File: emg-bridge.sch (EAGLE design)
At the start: 23 parts

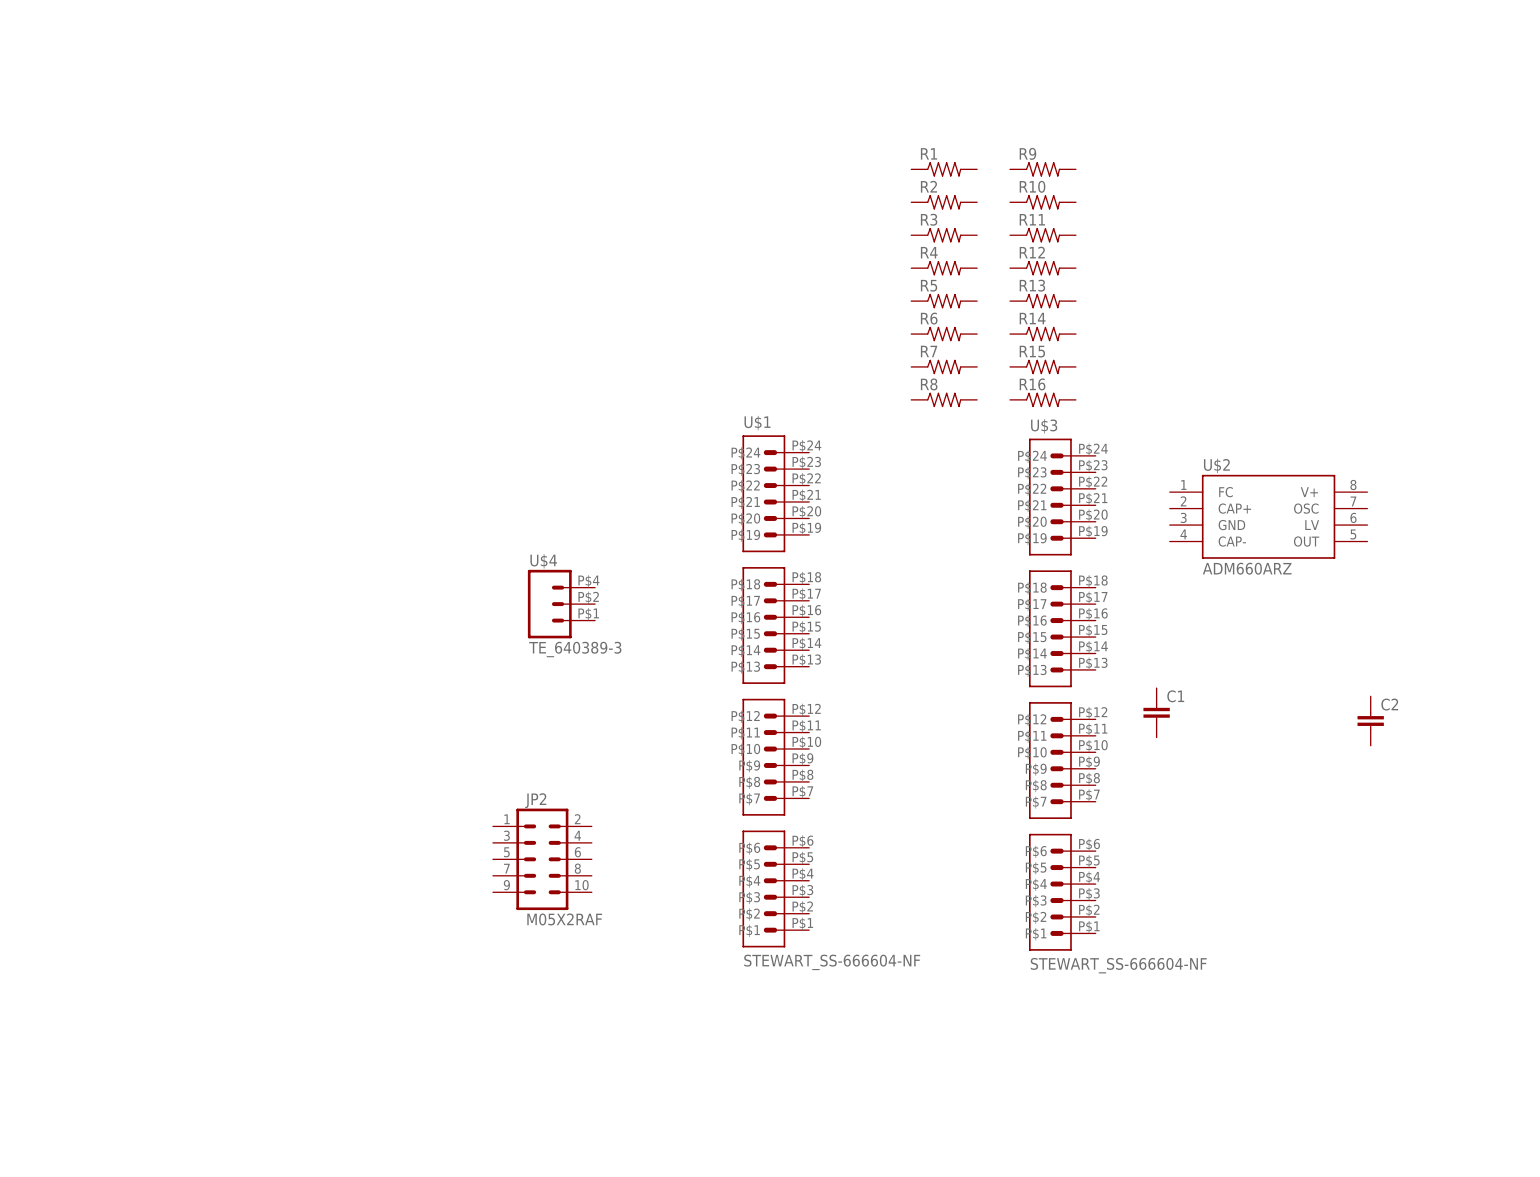
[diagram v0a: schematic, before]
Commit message: Updated parts from eagle-lib. Worked out pinouts for all connectors.
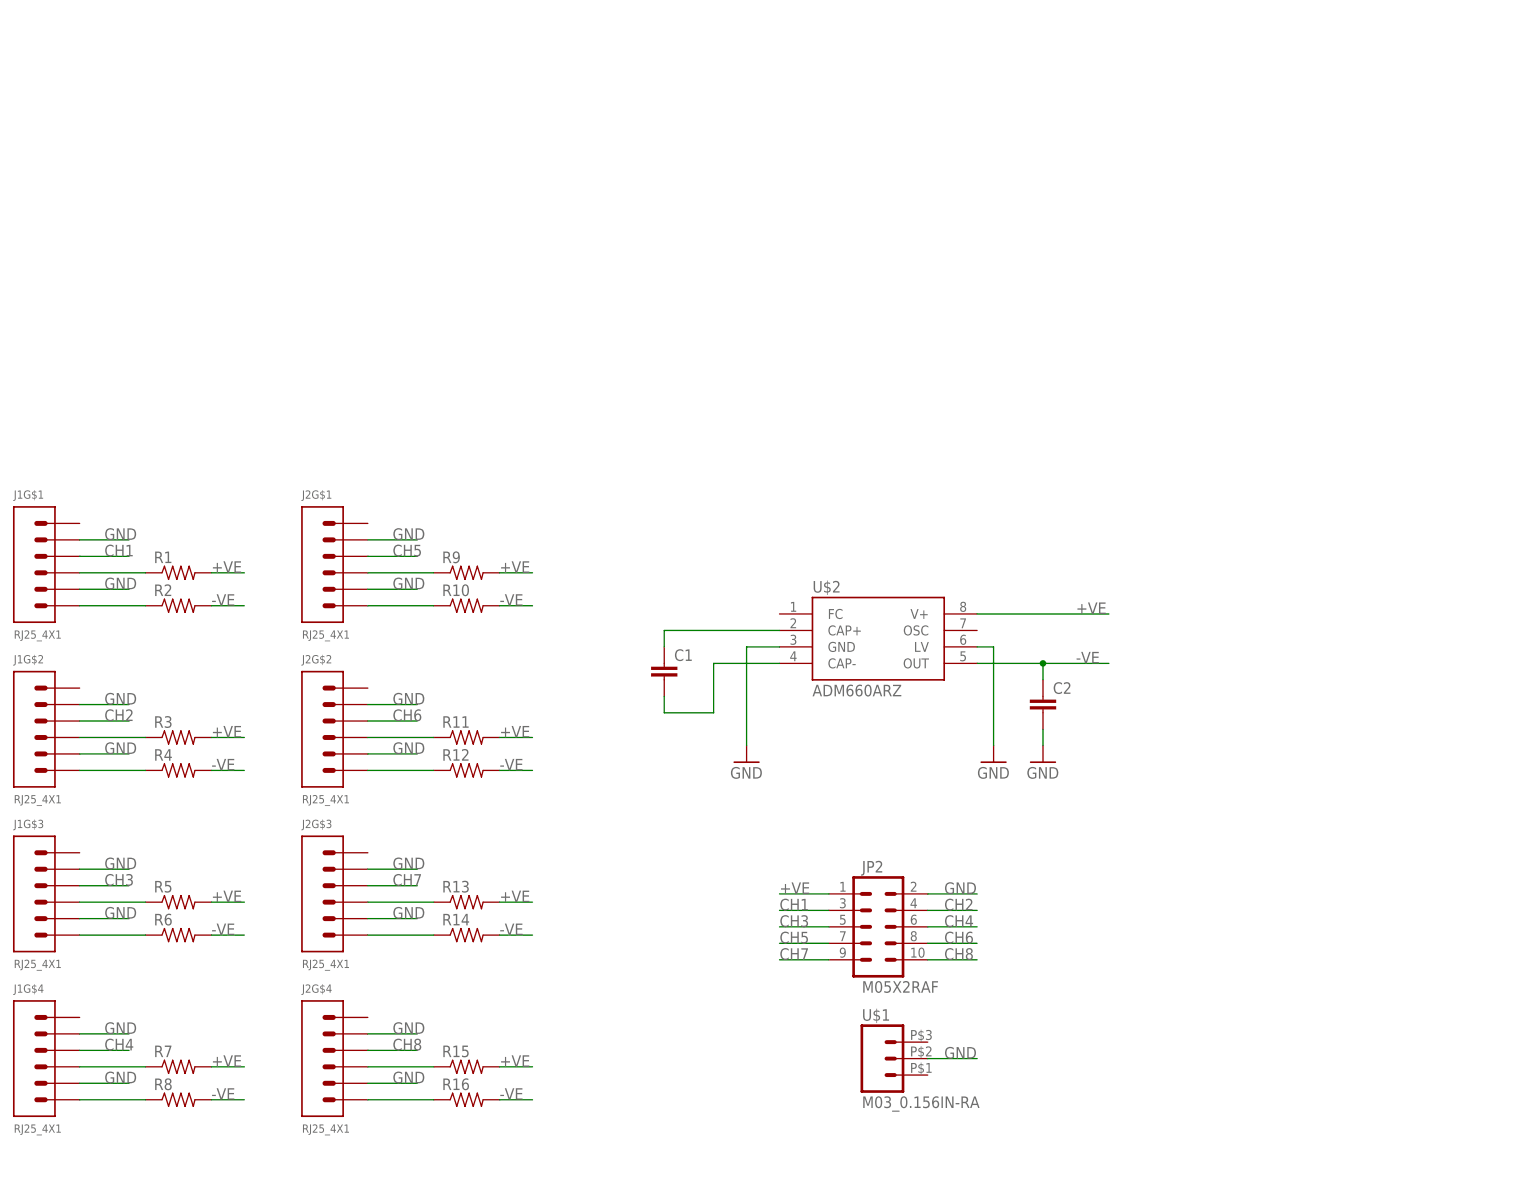
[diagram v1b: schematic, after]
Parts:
- removed U$3: STEWART_SS-666604-NF, eagle-lib:STEWART_SS-666604-NF
- removed U$4: TE_640389-3, eagle-lib:TE_640389-3
- added J1, J2: RJ25_4X1, eagle-lib:RJ25_4X1
- U$1: value STEWART_SS-666604-NF -> M03_0.156IN-RA; device eagle-lib:STEWART_SS-666604-NF -> eagle-lib:M03_0.156IN-RA
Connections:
- new net +VE: JP2.1, R1.2, R11.2, R13.2, R15.2, R3.2, R5.2, R7.2, R9.2, U$2.V+
- new net -VE: C2.1, R10.2, R12.2, R14.2, R16.2, R2.2, R4.2, R6.2, R8.2, U$2.OUT
- new net CH1: J1G$1.P$4, JP2.3
- new net CH2: J1G$2.P$4, JP2.4
- new net CH3: J1G$3.P$4, JP2.5
- new net CH4: J1G$4.P$4, JP2.6
- new net CH5: J2G$1.P$4, JP2.7
- new net CH6: J2G$2.P$4, JP2.8
- new net CH7: J2G$3.P$4, JP2.9
- new net CH8: J2G$4.P$4, JP2.10
- new net GND: C2.2, J1G$1.P$2, J1G$1.P$5, J1G$2.P$2, J1G$2.P$5, J1G$3.P$2, J1G$3.P$5, J1G$4.P$2, J1G$4.P$5, J2G$1.P$2, J2G$1.P$5, J2G$2.P$2, J2G$2.P$5, J2G$3.P$2, J2G$3.P$5, J2G$4.P$2, J2G$4.P$5, JP2.2, U$1.2, U$2.GND, U$2.LV
- new net N$1: J1G$1.P$1, R2.1
- new net N$11: J1G$3.P$1, R6.1
- new net N$13: J1G$3.P$3, R5.1
- new net N$16: J1G$4.P$1, R8.1
- new net N$18: J1G$4.P$3, R7.1
- new net N$2: C1.2, U$2.CAP-
- new net N$21: J2G$1.P$1, R10.1
- new net N$23: J2G$1.P$3, R9.1
- new net N$26: J2G$2.P$1, R12.1
- new net N$28: J2G$2.P$3, R11.1
- new net N$3: J1G$1.P$3, R1.1
- new net N$31: J2G$3.P$1, R14.1
- new net N$33: J2G$3.P$3, R13.1
- new net N$36: J2G$4.P$1, R16.1
- new net N$38: J2G$4.P$3, R15.1
- new net N$4: C1.1, U$2.CAP+
- new net N$6: J1G$2.P$1, R4.1
- new net N$8: J1G$2.P$3, R3.1
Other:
- moved on the sheet: C1, C2, JP2, R1, R10, R11, R12, R13, R14, R15, R16, R2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

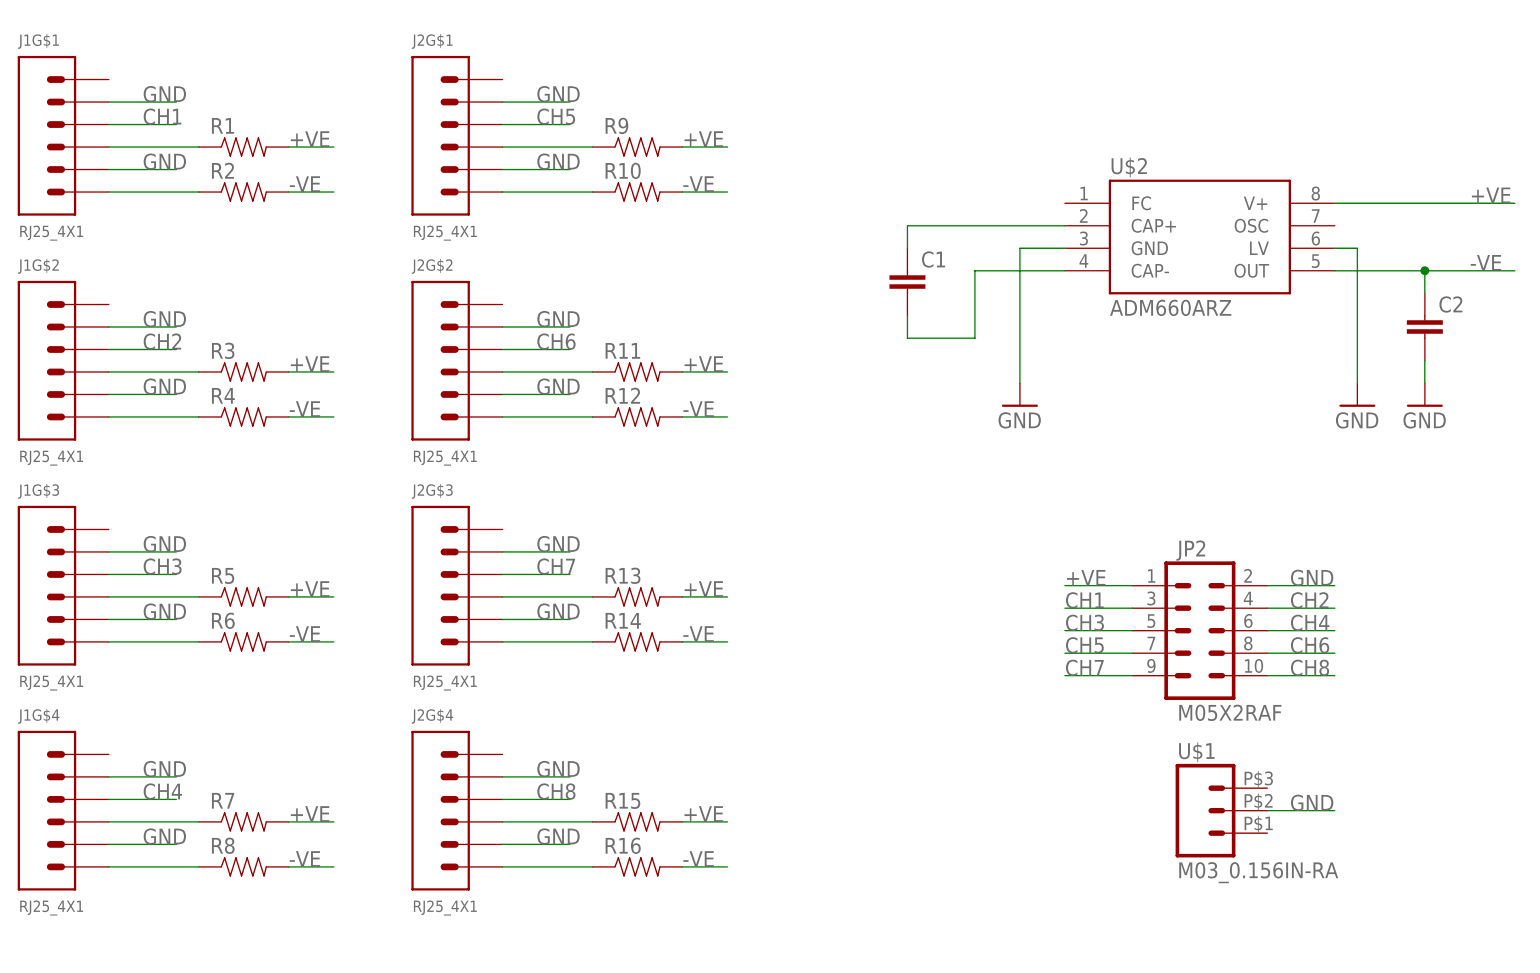
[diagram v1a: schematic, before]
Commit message: Schematic cleaned up and board layout/routing rough draft completed.
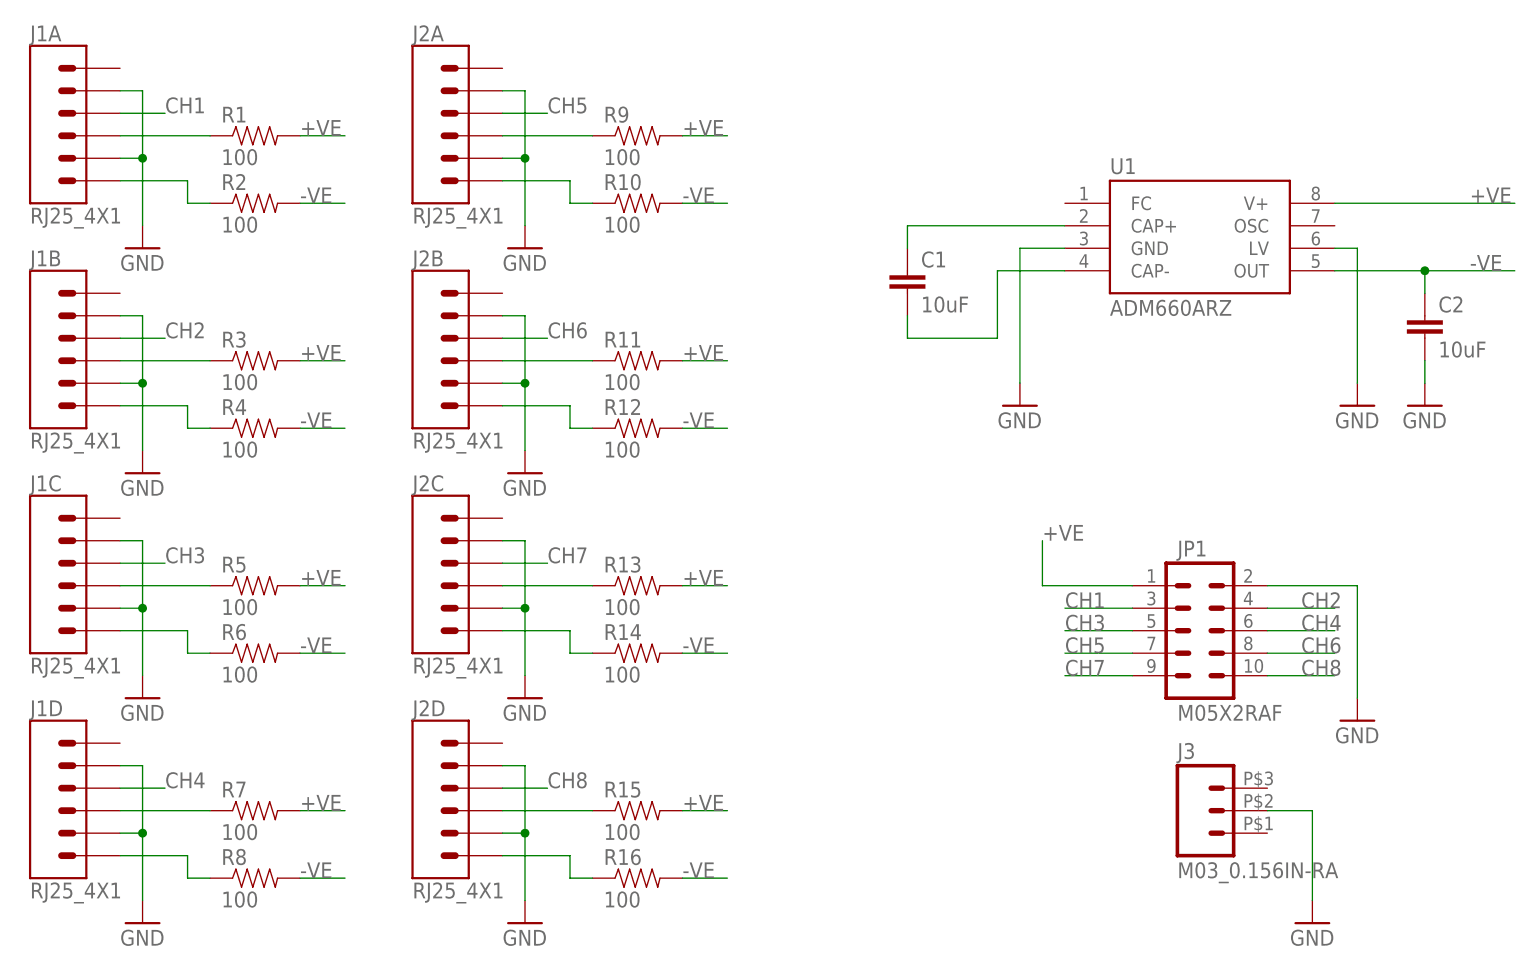
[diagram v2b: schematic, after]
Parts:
- C1, C2: value (none) -> 10uF
- R1, R10, R11, R12, R13, R14, R15, R16, R2, R3, R4, R5, R6, R7, R8, R9: value (none) -> 100
- renumbered JP2 to JP1, U$1 to J3, U$2 to U1
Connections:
- net CH1: now also J1A.P$4; no longer J1G$1.P$4
- net CH2: now also J1B.P$4; no longer J1G$2.P$4
- net CH3: now also J1C.P$4; no longer J1G$3.P$4
- net CH4: now also J1D.P$4; no longer J1G$4.P$4
- net CH5: now also J2A.P$4; no longer J2G$1.P$4
- net CH6: now also J2B.P$4; no longer J2G$2.P$4
- net CH7: now also J2C.P$4; no longer J2G$3.P$4
- net CH8: now also J2D.P$4; no longer J2G$4.P$4
- net GND: now also J1A.P$2, J1A.P$5, J1B.P$2, J1B.P$5, J1C.P$2, J1C.P$5, J1D.P$2, J1D.P$5, J2A.P$2, J2A.P$5, J2B.P$2, J2B.P$5, J2C.P$2, J2C.P$5, J2D.P$2, J2D.P$5; no longer J1G$1.P$2, J1G$1.P$5, J1G$2.P$2, J1G$2.P$5, J1G$3.P$2, J1G$3.P$5, J1G$4.P$2, J1G$4.P$5, J2G$1.P$2, J2G$1.P$5, J2G$2.P$2, J2G$2.P$5, J2G$3.P$2, J2G$3.P$5, J2G$4.P$2, J2G$4.P$5
- net N$1: now also J1A.P$1; no longer J1G$1.P$1
- net N$11: now also J1C.P$1; no longer J1G$3.P$1
- net N$13: now also J1C.P$3; no longer J1G$3.P$3
- net N$16: now also J1D.P$1; no longer J1G$4.P$1
- net N$18: now also J1D.P$3; no longer J1G$4.P$3
- net N$21: now also J2A.P$1; no longer J2G$1.P$1
- net N$23: now also J2A.P$3; no longer J2G$1.P$3
- net N$26: now also J2B.P$1; no longer J2G$2.P$1
- net N$28: now also J2B.P$3; no longer J2G$2.P$3
- net N$3: now also J1A.P$3; no longer J1G$1.P$3
- net N$31: now also J2C.P$1; no longer J2G$3.P$1
- net N$33: now also J2C.P$3; no longer J2G$3.P$3
- net N$36: now also J2D.P$1; no longer J2G$4.P$1
- net N$38: now also J2D.P$3; no longer J2G$4.P$3
- net N$6: now also J1B.P$1; no longer J1G$2.P$1
- net N$8: now also J1B.P$3; no longer J1G$2.P$3
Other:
- moved on the sheet: R1, R10, R11, R12, R13, R14, R15, R16, R2, R3, R4, R5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
